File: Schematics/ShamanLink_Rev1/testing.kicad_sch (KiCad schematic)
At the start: 28 parts, among them J2 Conn_02x05_Odd_Even

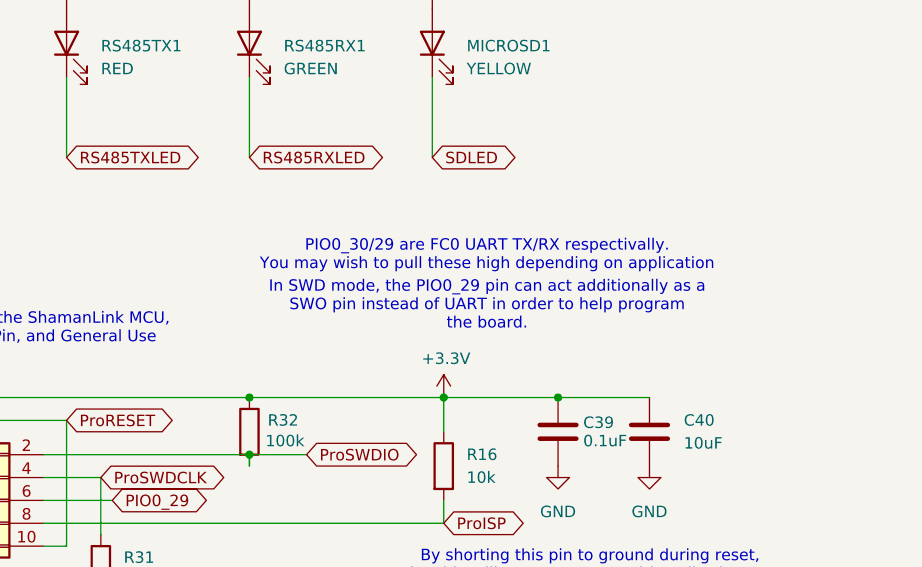
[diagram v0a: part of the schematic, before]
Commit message: Clarified SWO UART tradeoff implemenation
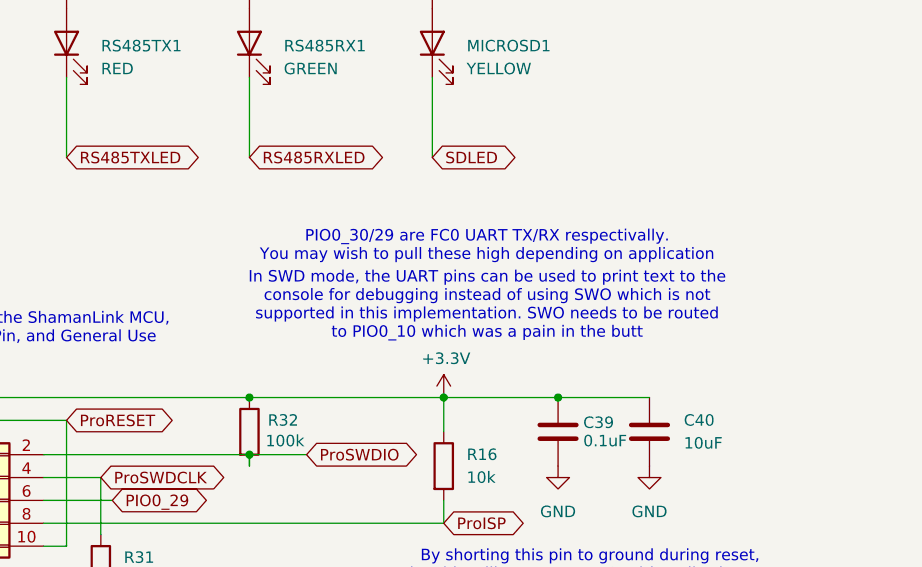
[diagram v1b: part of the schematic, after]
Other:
- note added: "In SWD mode, the UART pins can be used to print text to the console for debugging instead of using SWO which is not supported in this implementation. SWO needs to be routed to PIO0_10 which was a pain in the butt"
- note removed: "In SWD mode, the PIO0_29 pin can act additionally as a SWO pin instead of UART in order to help program the board."
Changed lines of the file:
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@@
 		)
 	)
-	(text "In SWD mode, the PIO0_29 pin can act additionally as a \nSWO pin instead of UART in order to help program\nthe board. "
+	(text "In SWD mode, the UART pins can be used to print text to the\nconsole for debugging instead of using SWO which is not \nsupported in this implementation. SWO needs to be routed \nto PIO0_10 which was a pain in the butt"
 		(exclude_from_sim no)
 		(at 242.316 78.74 0)
@@
 	(text "PIO0_30/29 are FC0 UART TX/RX respectivally.\nYou may wish to pull these high depending on application"
 		(exclude_from_sim no)
-		(at 242.316 73.152 0)
+		(at 242.316 72.136 0)
 		(effects
 			(font

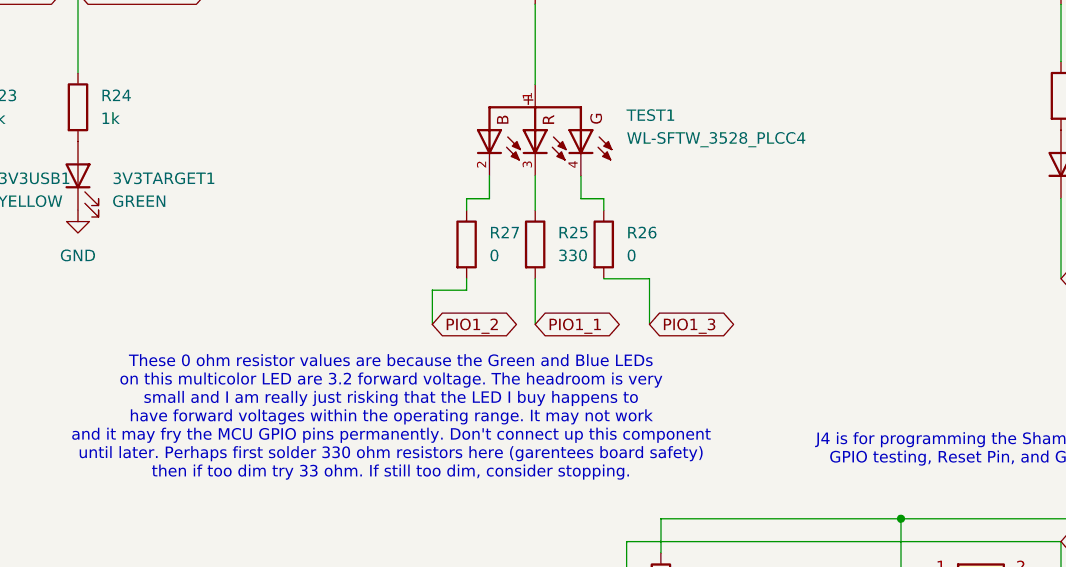
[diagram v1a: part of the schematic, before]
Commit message: Final ShamanLink Revisions and Motor Totem Final Revisions
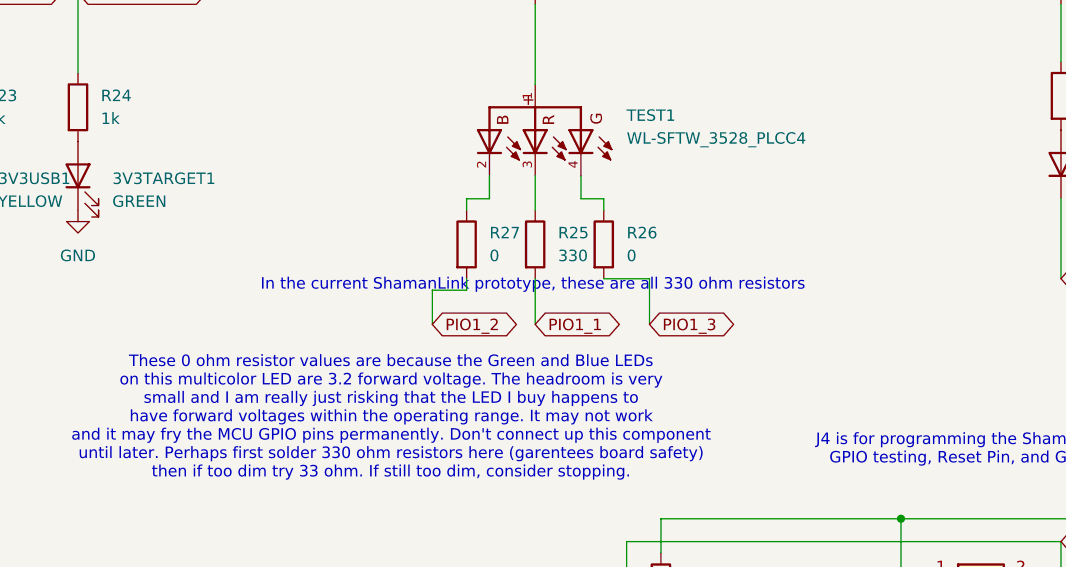
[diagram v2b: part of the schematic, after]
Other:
- note added: "In the current ShamanLink prototype, these are all 330 ohm resistors"
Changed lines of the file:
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@@
+		)
+	)
+	(text "In the current ShamanLink prototype, these are all 330 ohm resistors"
+		(exclude_from_sim no)
+		(at 136.906 62.992 0)
+		(effects
+			(font
+				(size 1.27 1.27)
+			)
 		)
 	)
